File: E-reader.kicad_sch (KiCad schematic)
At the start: 0 parts

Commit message: added the rpi cm4 100 high density connectors to a library and getting started on building the base of the carrier board to allow for further iteration
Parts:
- added U1: CM4008032B, CM4008032B:MODULE_CM4008032B, symbol CM4008032B:CM4008032B
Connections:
- new net: U1.104 (RESERVED), U1.106 (RESERVED), U1.76 (RESERVED)
- new net: U1.SH1 (MOUNTING_PADS), U1.SH2 (MOUNTING_PADS), U1.SH3 (MOUNTING_PADS), U1.SH4 (MOUNTING_PADS)
- new net +5V(INPUT): U1.77 (+5V(INPUT)), U1.79 (+5V(INPUT)), U1.81 (+5V(INPUT)), U1.83 (+5V(INPUT)), U1.85 (+5V(INPUT)), U1.87 (+5V(INPUT))
- new net CM4_1.8V(OUTPUT): U1.88 (CM4_1.8V(OUTPUT)), U1.90 (CM4_1.8V(OUTPUT))
- new net CM4_3.3V(OUTPUT): U1.84 (CM4_3.3V(OUTPUT)), U1.86 (CM4_3.3V(OUTPUT))
- new net GND: U1.1 (GND), U1.107 (GND), U1.108 (GND), U1.113 (GND), U1.114 (GND), U1.119 (GND), U1.120 (GND), U1.125 (GND), U1.126 (GND), U1.13 (GND), U1.131 (GND), U1.132 (GND), U1.137 (GND), U1.138 (GND), U1.14 (GND), U1.144 (GND), U1.150 (GND), U1.155 (GND), U1.156 (GND), U1.161 (GND), U1.162 (GND), U1.167 (GND), U1.168 (GND), U1.173 (GND), U1.174 (GND), U1.179 (GND), U1.180 (GND), U1.185 (GND), U1.186 (GND), U1.191 (GND), U1.192 (GND), U1.197 (GND), U1.198 (GND), U1.2 (GND), U1.22 (GND), U1.23 (GND), U1.32 (GND), U1.33 (GND), U1.42 (GND), U1.43 (GND), U1.52 (GND), U1.53 (GND), U1.59 (GND), U1.60 (GND), U1.65 (GND), U1.66 (GND), U1.7 (GND), U1.71 (GND), U1.74 (GND), U1.8 (GND), U1.98 (GND)
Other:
- title: (none) -> Soquartz wiring 

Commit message: idk, it had changes to commit
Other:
- added sheet Power management (PowerManagement.kicad_sch)
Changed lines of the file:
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@@
+		)
+	)
+	(sheet
+		(at 15.24 171.45)
+		(size 17.78 21.59)
+		(exclude_from_sim no)
+		(in_bom yes)
+		(on_board yes)
+		(dnp no)
+		(fields_autoplaced yes)
+		(stroke
+			(width 0.1524)
+			(type solid)
+		)
+		(fill
+			(color 0 0 0 0)
+		)
+		(property "Sheetname" "Power management"
+			(at 15.24 170.7384 0)
+			(show_name no)
+			(do_not_autoplace no)
+			(effects
+				(font
+					(size 1.27 1.27)
+				)
+				(justify left bottom)
+			)
+		)
+		(property "Sheetfile" "PowerManagement.kicad_sch"
+			(at 15.24 193.6246 0)
+			(show_name no)
+			(do_not_autoplace no)
+			(effects
+				(font
+					(size 1.27 1.27)
+				)
+				(justify left top)
+			)
+		)
+		(instances
+			(project "E-reader"
+				(path "/bcc0a360-382d-49a3-9cc2-bd35b82cdeaa"
+					(page "2")
+				)
+			)
 		)
 	)

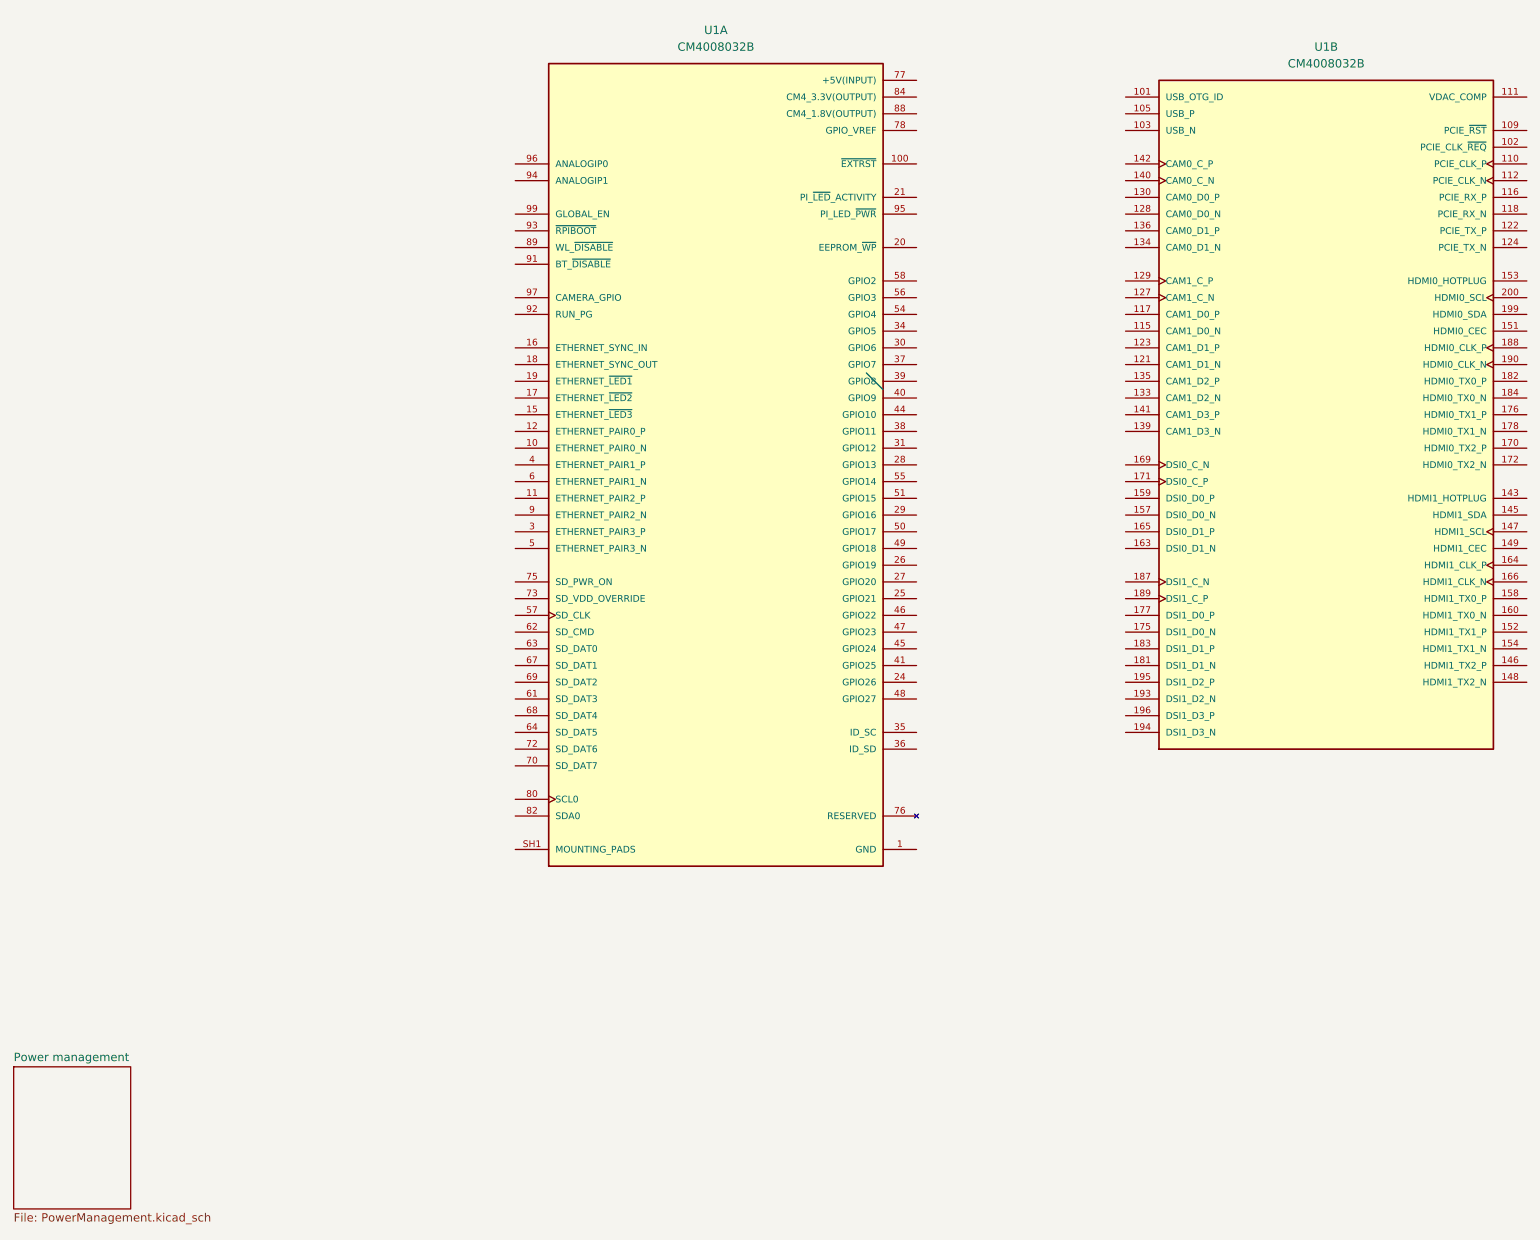
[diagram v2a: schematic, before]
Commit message: adding USB-C port for charging and data transfer
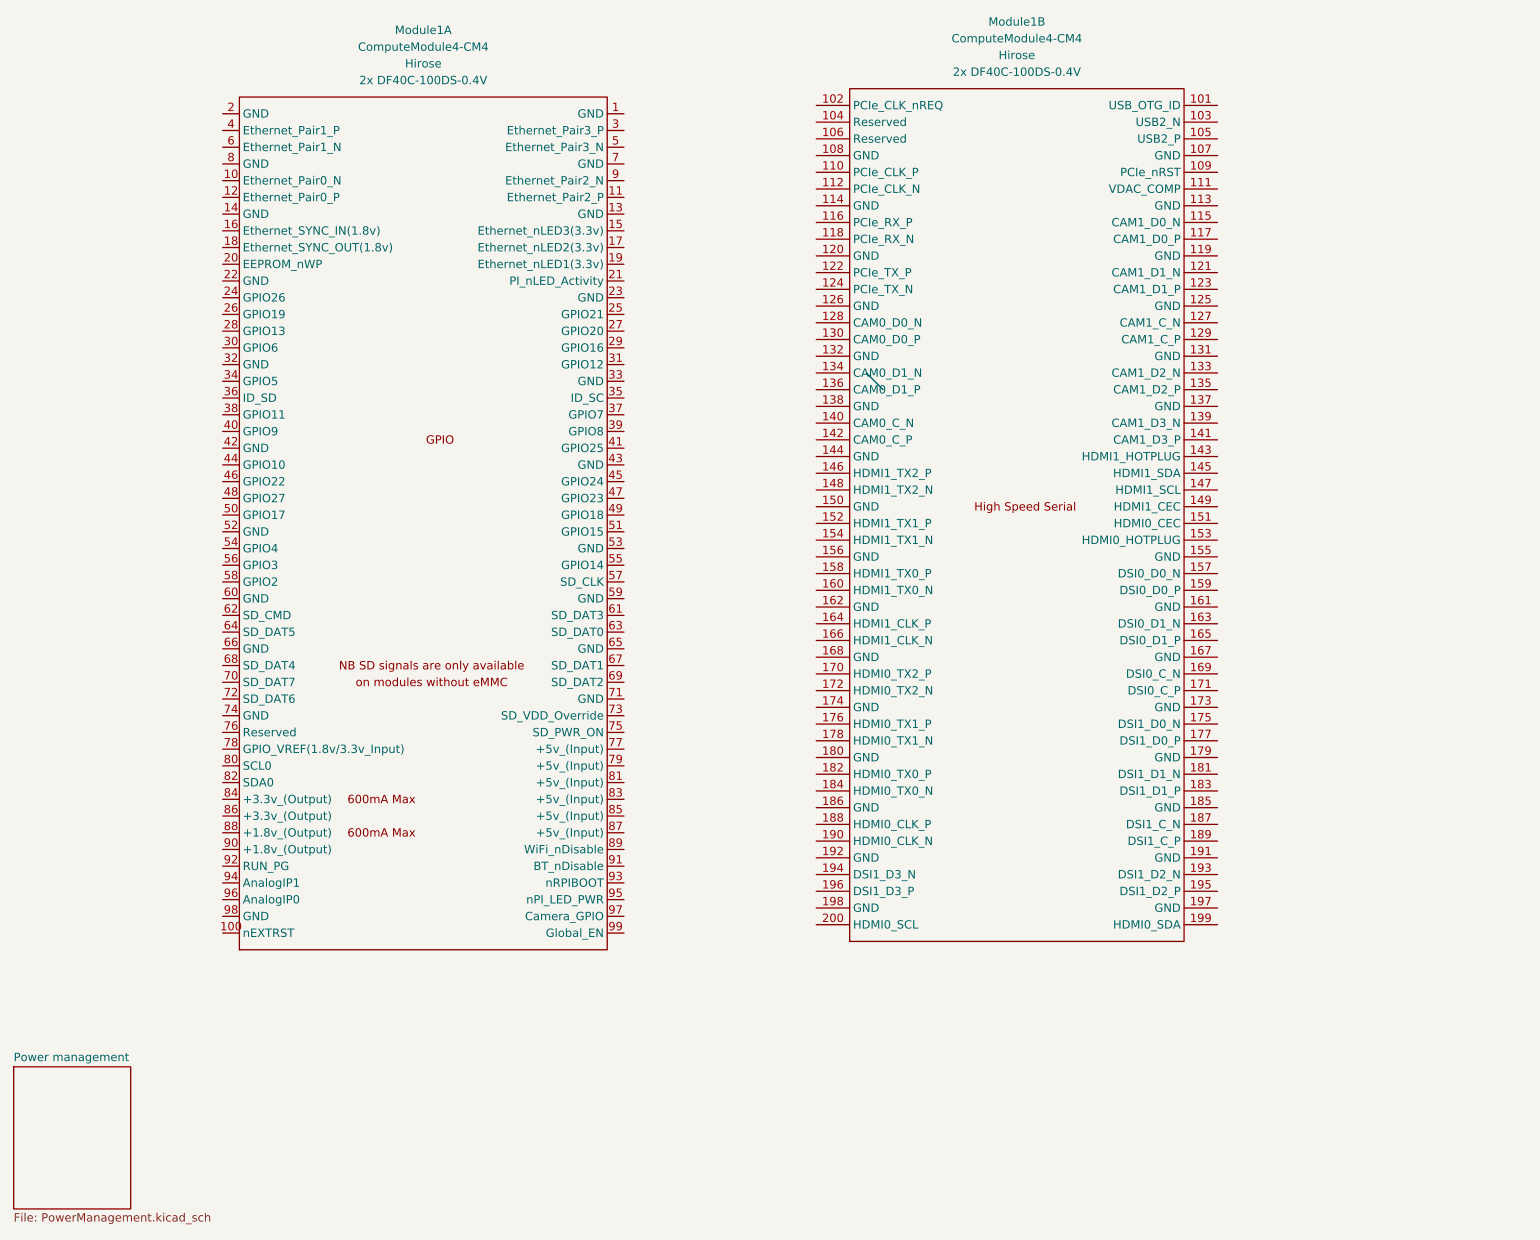
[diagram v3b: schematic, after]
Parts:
- removed U1: CM4008032B, CM4008032B:MODULE_CM4008032B, symbol CM4008032B:CM4008032B
- added Module1: ComputeModule4-CM4, CM4IO:Raspberry-Pi-4-Compute-Module, symbol CM4IO:ComputeModule4-CM4
